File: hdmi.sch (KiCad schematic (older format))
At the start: 31 parts, among them J1901 Mini-HDMI, Q1901 NX3020NAKS, Q1902 NX3020NAKS, Q1903 NX3020NAKS, Q1904 NX3020NAKS, U1901 PCMF3HDMI2SZ, U1902 PCMF2HDMI2SZ

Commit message: Assign TLV3201AIDBVR footprint based on the SOT-23-5 official footprint using the given solder mask clearance and pad clearance parameters, assign the QFN48 3D model to the ETH PHY footprint, make some minor adjustments to the front sheet's layout
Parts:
- renumbered Q1903 to Q1901, Q1901 to Q1902, Q1903 to Q1902, Q1902 to Q1903, Q1904 to Q1903, Q1902 to Q1904
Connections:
- net 1V8_P: now also Q1901.5 (G), Q1902.2 (G), Q1903.5 (G), Q1904.2 (G); no longer Q1901.2 (G), Q1902.5 (G), Q1903.2 (G), Q1904.5 (G)
- net GND: now also Q1901.4 (S), Q1902.1 (S), Q1903.4 (S), Q1904.1 (S); no longer Q1901.1 (S), Q1902.4 (S), Q1903.1 (S), Q1904.4 (S)
- net at R1903.2: now also Q1901.3 (D); no longer Q1902.3 (D)
- net at R1905.2: now also Q1902.6 (D); no longer Q1903.6 (D)
- net at R1907.2: now also Q1902.3 (D); no longer Q1904.3 (D)
- net at R1902.2: now also Q1903.6 (D); no longer Q1901.6 (D)
- net at R1904.2: now also Q1903.3 (D); no longer Q1902.3 (D)
- net at R1906.2: now also Q1904.6 (D); no longer Q1903.6 (D)
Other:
- moved on the sheet: Q1902B, Q1903A
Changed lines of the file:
@@
 Sheet 19 24
 Title "HDMI"
-Date "2018-06-11"
+Date "2018-06-14"
 Rev "v0.1.0"
 Comp "Copyright 2018 GNU GPLv3"
@@
 $EndComp
 $Comp
-L 1V8_P #PWR0329
+L 1V8_P #PWR1901
 U 1 1 5B01672B
 P 750 3350
-F 0 "#PWR0329" H 750 3200 50  0001 C CNN
+F 0 "#PWR1901" H 750 3200 50  0001 C CNN
 F 1 "1V8_P" H 750 3490 50  0000 C CNN
 F 2 "" H 750 3350 50  0001 C CNN
@@
 $EndComp
 $Comp
-L 1V8_P #PWR0330
+L 1V8_P #PWR1902
 U 1 1 5B019D66
 P 750 5050
-F 0 "#PWR0330" H 750 4900 50  0001 C CNN
+F 0 "#PWR1902" H 750 4900 50  0001 C CNN
 F 1 "1V8_P" H 750 5190 50  0000 C CNN
 F 2 "" H 750 5050 50  0001 C CNN
@@
 ±1%!!!
 $Comp
-L GND #PWR0331
+L GND #PWR1903
 U 1 1 5B081BE1
 P 4150 3400
-F 0 "#PWR0331" H 4150 3150 50  0001 C CNN
+F 0 "#PWR1903" H 4150 3150 50  0001 C CNN
 F 1 "GND" H 4150 3250 50  0000 C CNN
 F 2 "" H 4150 3400 50  0001 C CNN
@@
 HDMI_TX1N
 $Comp
-L GND #PWR0332
+L GND #PWR1904
 U 1 1 5B08911B
 P 4150 5100
-F 0 "#PWR0332" H 4150 4850 50  0001 C CNN
+F 0 "#PWR1904" H 4150 4850 50  0001 C CNN
 F 1 "GND" H 4150 4950 50  0000 C CNN
 F 2 "" H 4150 5100 50  0001 C CNN
@@
 Layout Note:\nMay need swap some signals\ndue to micro-HDMI pinout diff\ndepending on pin location/routing
 $Comp
-L GND #PWR0333
+L GND #PWR1908
 U 1 1 5AF69B9C
 P 9200 4900
-F 0 "#PWR0333" H 9200 4650 50  0001 C CNN
+F 0 "#PWR1908" H 9200 4650 50  0001 C CNN
 F 1 "GND" H 9200 4750 50  0000 C CNN
 F 2 "" H 9200 4900 50  0001 C CNN
@@
 $EndComp
 $Comp
-L GND #PWR0334
+L GND #PWR1906
 U 1 1 5AFABCE1
 P 6150 2400
-F 0 "#PWR0334" H 6150 2150 50  0001 C CNN
+F 0 "#PWR1906" H 6150 2150 50  0001 C CNN
 F 1 "GND" H 6150 2250 50  0000 C CNN
 F 2 "" H 6150 2400 50  0001 C CNN
@@
 $EndComp
 $Comp
-L 3V3_P #PWR0335
+L 3V3_P #PWR1907
 U 1 1 5AFBD440
 P 9200 1650
-F 0 "#PWR0335" H 9200 1500 50  0001 C CNN
+F 0 "#PWR1907" H 9200 1500 50  0001 C CNN
 F 1 "3V3_P" H 9200 1790 50  0000 C CNN
 F 2 "" H 9200 1650 50  0001 C CNN
@@
 $EndComp
 $Comp
-L 5V_P #PWR0336
+L 5V_P #PWR1905
 U 1 1 5B3E4E0C
 P 6050 1800
-F 0 "#PWR0336" H 6050 1650 50  0001 C CNN
+F 0 "#PWR1905" H 6050 1650 50  0001 C CNN
 F 1 "5V_P" H 6050 1940 50  0000 C CNN
 F 2 "" H 6050 1800 50  0001 C CNN
@@
 $EndComp
 $Comp
+L Q_NMOS_DUAL Q1901
+U 2 1 5B1A7CAB
+P 1900 3100
+F 0 "Q1901" H 1550 3300 50  0000 L CNN
+F 1 "NX3020NAKS" H 1350 3200 50  0000 L CNN
+F 2 "dvk-mx8m-bsb:6-TSSOP" H 2100 3200 50  0001 C CNN
+F 3 "https://assets.nexperia.com/documents/data-sheet/NX3020NAKS.pdf" H 1900 3100 50  0001 C CNN
+F 4 "NXP" H 1900 3100 60  0001 C CNN "MFG Name"
+F 5 "NX3020NAKS" H 1900 3100 60  0001 C CNN "MFG Part Num"
+F 6 "NX3020NAKS,115" H 1900 3100 60  0001 C CNN "Distrib PN"
+F 7 "https://www.arrow.com/en/products/nx3020naks115/nexperia" H 1900 3100 60  0001 C CNN "Distrib Link"
+F 8 "-" H 1900 3100 60  0001 C CNN "Tolerance"
+F 9 "https://octopart.com/search?q=NX3020NAKS&start=0" H 1900 3100 60  0001 C CNN "Others"
+	2    1900 3100
+	1    0    0    -1
+$EndComp
+$Comp
+L Q_NMOS_DUAL Q1902
+U 1 1 5B1A8769
+P 2650 3100
+F 0 "Q1902" H 2300 3300 50  0000 L CNN
+F 1 "NX3020NAKS" H 2100 3200 50  0000 L CNN
+F 2 "dvk-mx8m-bsb:6-TSSOP" H 2850 3200 50  0001 C CNN
+F 3 "https://assets.nexperia.com/documents/data-sheet/NX3020NAKS.pdf" H 2650 3100 50  0001 C CNN
+F 4 "NXP" H 2650 3100 60  0001 C CNN "MFG Name"
+F 5 "NX3020NAKS" H 2650 3100 60  0001 C CNN "MFG Part Num"
+F 6 "NX3020NAKS,115" H 2650 3100 60  0001 C CNN "Distrib PN"
+F 7 "https://www.arrow.com/en/products/nx3020naks115/nexperia" H 2650 3100 60  0001 C CNN "Distrib Link"
+F 8 "-" H 2650 3100 60  0001 C CNN "Tolerance"
+F 9 "https://octopart.com/search?q=NX3020NAKS&start=0" H 2650 3100 60  0001 C CNN "Others"
+	1    2650 3100
+	1    0    0    -1
+$EndComp
+$Comp
 L Q_NMOS_DUAL Q1903
-U 1 1 5B1A7CAB
+U 1 1 5B1A87F5
 P 1150 4800
 F 0 "Q1903" H 800 5000 50  0000 L CNN
@@
 $EndComp
 $Comp
-L Q_NMOS_DUAL Q1901
-U 2 1 5B1A8769
-P 1900 3100
-F 0 "Q1901" H 1550 3300 50  0000 L CNN
-F 1 "NX3020NAKS" H 1350 3200 50  0000 L CNN
-F 2 "dvk-mx8m-bsb:6-TSSOP" H 2100 3200 50  0001 C CNN
-F 3 "https://assets.nexperia.com/documents/data-sheet/NX3020NAKS.pdf" H 1900 3100 50  0001 C CNN
-F 4 "NXP" H 1900 3100 60  0001 C CNN "MFG Name"
-F 5 "NX3020NAKS" H 1900 3100 60  0001 C CNN "MFG Part Num"
-F 6 "NX3020NAKS,115" H 1900 3100 60  0001 C CNN "Distrib PN"
-F 7 "https://www.arrow.com/en/products/nx3020naks115/nexperia" H 1900 3100 60  0001 C CNN "Distrib Link"
-F 8 "-" H 1900 3100 60  0001 C CNN "Tolerance"
-F 9 "https://octopart.com/search?q=NX3020NAKS&start=0" H 1900 3100 60  0001 C CNN "Others"
-	2    1900 3100
+L Q_NMOS_DUAL Q1904
+U 1 1 5B1A8AD3
+P 2650 4800
+F 0 "Q1904" H 2300 5000 50  0000 L CNN
+F 1 "NX3020NAKS" H 2100 4900 50  0000 L CNN
+F 2 "dvk-mx8m-bsb:6-TSSOP" H 2850 4900 50  0001 C CNN
+F 3 "https://assets.nexperia.com/documents/data-sheet/NX3020NAKS.pdf" H 2650 4800 50  0001 C CNN
+F 4 "NXP" H 2650 4800 60  0001 C CNN "MFG Name"
+F 5 "NX3020NAKS" H 2650 4800 60  0001 C CNN "MFG Part Num"
+F 6 "NX3020NAKS,115" H 2650 4800 60  0001 C CNN "Distrib PN"
+F 7 "https://www.arrow.com/en/products/nx3020naks115/nexperia" H 2650 4800 60  0001 C CNN "Distrib Link"
+F 8 "-" H 2650 4800 60  0001 C CNN "Tolerance"
+F 9 "https://octopart.com/search?q=NX3020NAKS&start=0" H 2650 4800 60  0001 C CNN "Others"
+	1    2650 4800
 	1    0    0    -1
 $EndComp
 $Comp
 L Q_NMOS_DUAL Q1902
-U 1 1 5B1A87F5
-P 2650 3100
-F 0 "Q1902" H 2300 3300 50  0000 L CNN
-F 1 "NX3020NAKS" H 2100 3200 50  0000 L CNN
-F 2 "dvk-mx8m-bsb:6-TSSOP" H 2850 3200 50  0001 C CNN
-F 3 "https://assets.nexperia.com/documents/data-sheet/NX3020NAKS.pdf" H 2650 3100 50  0001 C CNN
-F 4 "NXP" H 2650 3100 60  0001 C CNN "MFG Name"
-F 5 "NX3020NAKS" H 2650 3100 60  0001 C CNN "MFG Part Num"
-F 6 "NX3020NAKS,115" H 2650 3100 60  0001 C CNN "Distrib PN"
-F 7 "https://www.arrow.com/en/products/nx3020naks115/nexperia" H 2650 3100 60  0001 C CNN "Distrib Link"
-F 8 "-" H 2650 3100 60  0001 C CNN "Tolerance"
-F 9 "https://octopart.com/search?q=NX3020NAKS&start=0" H 2650 3100 60  0001 C CNN "Others"
-	1    2650 3100
-	1    0    0    -1
-$EndComp
-$Comp
-L Q_NMOS_DUAL Q1902
-U 2 1 5B1A8AD3
+U 2 1 5B1A9D21
 P 3400 3100
 F 0 "Q1902" H 3050 3300 50  0000 L CNN
@@
 $Comp
 L Q_NMOS_DUAL Q1903
-U 2 1 5B1A9D21
+U 2 1 5B1A9DC4
 P 1900 4800
 F 0 "Q1903" H 1550 5000 50  0000 L CNN
@@
 	1    0    0    -1
 $EndComp
-$Comp
-L Q_NMOS_DUAL Q1904
-U 1 1 5B1A9DC4
-P 2650 4800
-F 0 "Q1904" H 2300 5000 50  0000 L CNN
-F 1 "NX3020NAKS" H 2100 4900 50  0000 L CNN
-F 2 "dvk-mx8m-bsb:6-TSSOP" H 2850 4900 50  0001 C CNN
-F 3 "https://assets.nexperia.com/documents/data-sheet/NX3020NAKS.pdf" H 2650 4800 50  0001 C CNN
-F 4 "NXP" H 2650 4800 60  0001 C CNN "MFG Name"
-F 5 "NX3020NAKS" H 2650 4800 60  0001 C CNN "MFG Part Num"
-F 6 "NX3020NAKS,115" H 2650 4800 60  0001 C CNN "Distrib PN"
-F 7 "https://www.arrow.com/en/products/nx3020naks115/nexperia" H 2650 4800 60  0001 C CNN "Distrib Link"
-F 8 "-" H 2650 4800 60  0001 C CNN "Tolerance"
-F 9 "https://octopart.com/search?q=NX3020NAKS&start=0" H 2650 4800 60  0001 C CNN "Others"
-	1    2650 4800
-	1    0    0    -1
-$EndComp

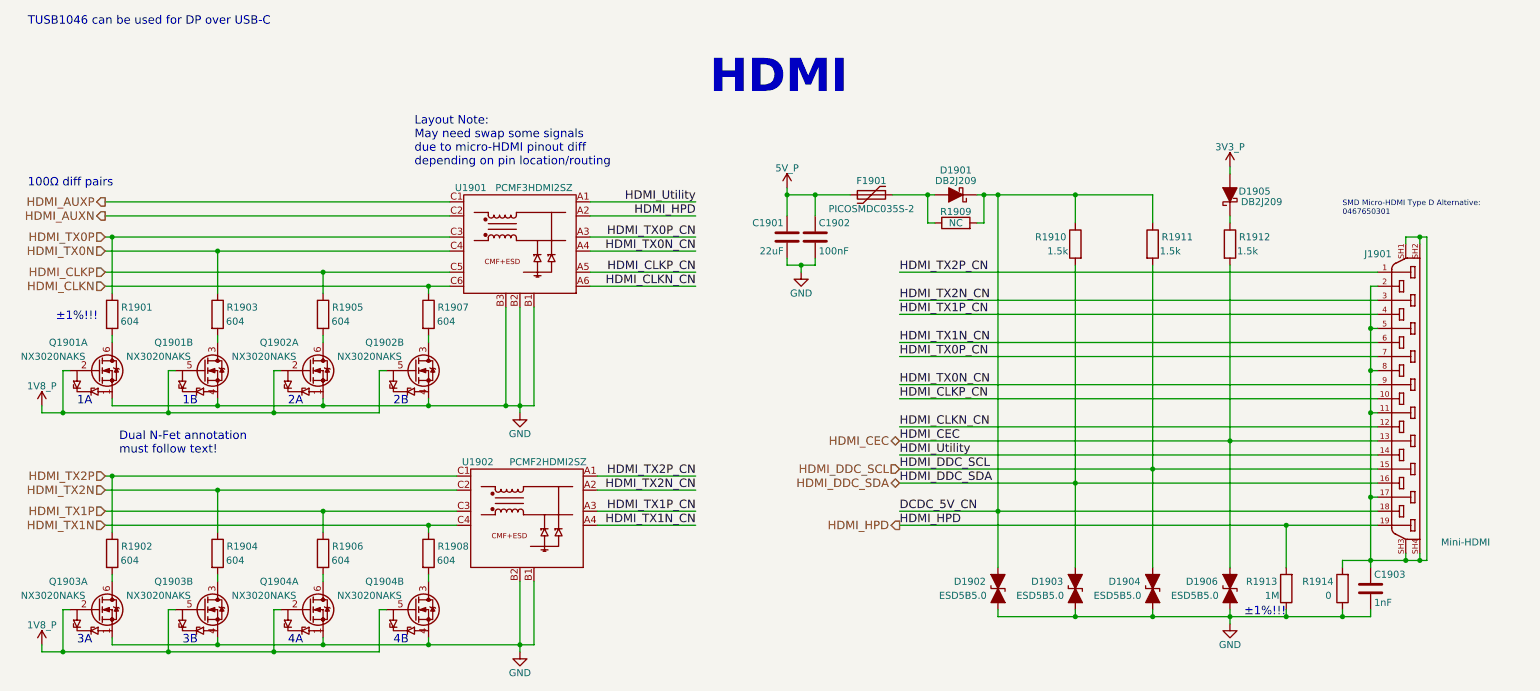
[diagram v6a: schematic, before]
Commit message: Add AC coupling caps to the HDMI_AUXP/N diff pair which were mistakenly left out, fix a couple typos/errors that were made when transitioning to the new top-leve sheet, make the M.2s' I2C RX TX hierarchical signals consistent and clearer
Hopefully all lingering errors have been caught, this will likely be the schematic commit that gets reviewed (fingers crossed).
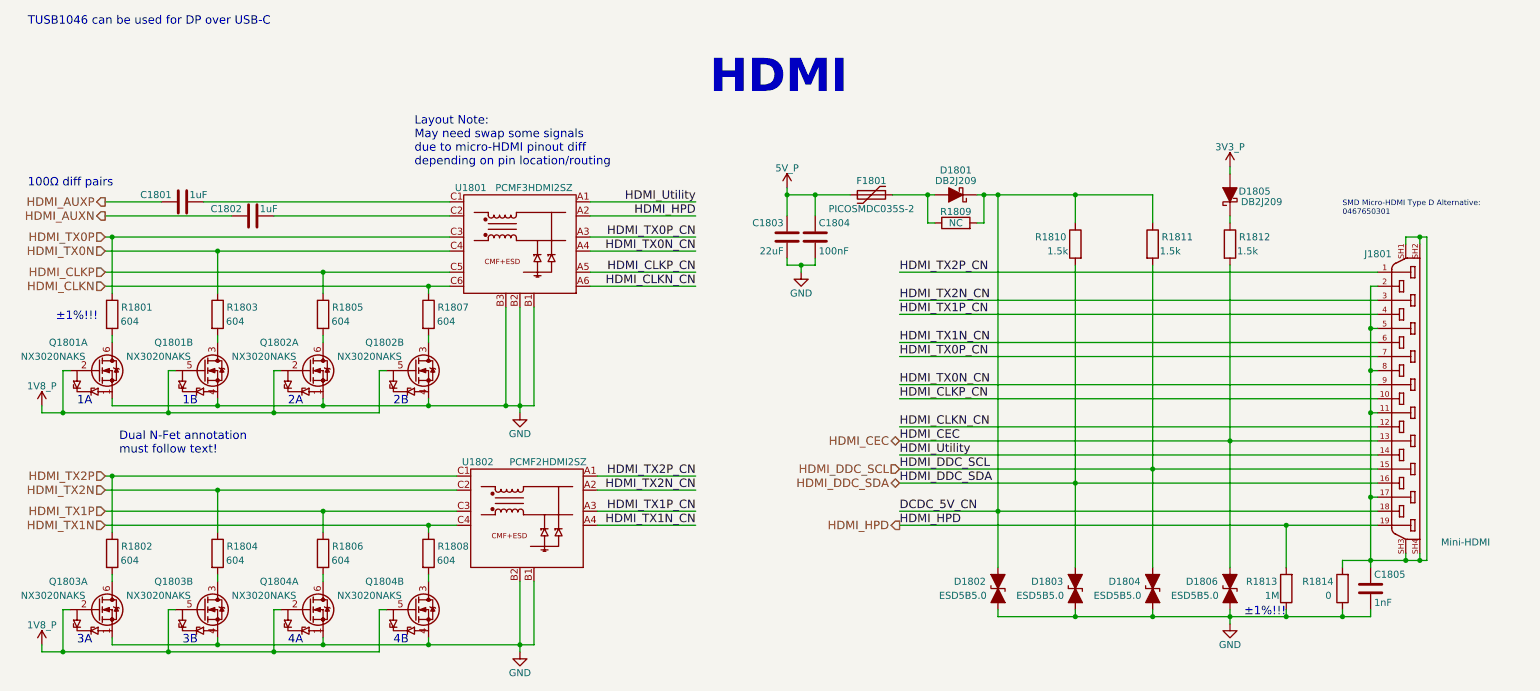
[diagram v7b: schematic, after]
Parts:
- added C1801, C1802: 1uF, symbol C
- renumbered C1901 to C1803, C1902 to C1804, C1903 to C1805, D1901 to D1801, D1902 to D1802, D1903 to D1803, D1904 to D1804, D1905 to D1805, D1906 to D1806, F1901 to F1801, J1901 to J1801, Q1901 to Q1801, Q1903 to Q1801, Q1901 to Q1802, Q1903 to Q1802, Q1902 to Q1803, Q1904 to Q1803, Q1902 to Q1804, Q1904 to Q1804, R1901 to R1801, R1902 to R1802, R1903 to R1803, R1904 to R1804, R1905 to R1805, R1906 to R1806, R1907 to R1807, R1908 to R1808, R1909 to R1809, R1910 to R1810, R1911 to R1811, R1912 to R1812, R1913 to R1813, R1914 to R1814, U1901 to U1801, U1902 to U1802
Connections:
- net 1V8_P: now also Q1801.5 (G), Q1802.2 (G), Q1803.5 (G), Q1804.2 (G); no longer Q1801.2 (G), Q1802.5 (G), Q1803.2 (G), Q1804.5 (G)
- net GND: now also Q1801.4 (S), Q1802.1 (S), Q1803.4 (S), Q1804.1 (S); no longer Q1801.1 (S), Q1802.4 (S), Q1803.1 (S), Q1804.4 (S)
- net HDMI_AUXN: now also C1802.2; no longer U1801.C2
- net HDMI_AUXP: now also C1801.2; no longer U1801.C1
- net at R1803.2: now also Q1801.3 (D); no longer Q1802.3 (D)
- net at R1805.2: now also Q1802.6 (D); no longer Q1803.6 (D)
- net at R1807.2: now also Q1802.3 (D); no longer Q1804.3 (D)
- net at R1802.2: now also Q1803.6 (D); no longer Q1801.6 (D)
- net at R1804.2: now also Q1803.3 (D); no longer Q1802.3 (D)
- net at R1806.2: now also Q1804.6 (D); no longer Q1803.6 (D)
- new net: C1801.1, U1801.C1
- new net: C1802.1, U1801.C2
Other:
- moved on the sheet: Q1802B, Q1803A

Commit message: Move the WLAN+BT M.2 sheet back to page 18 rather than the last page (24)
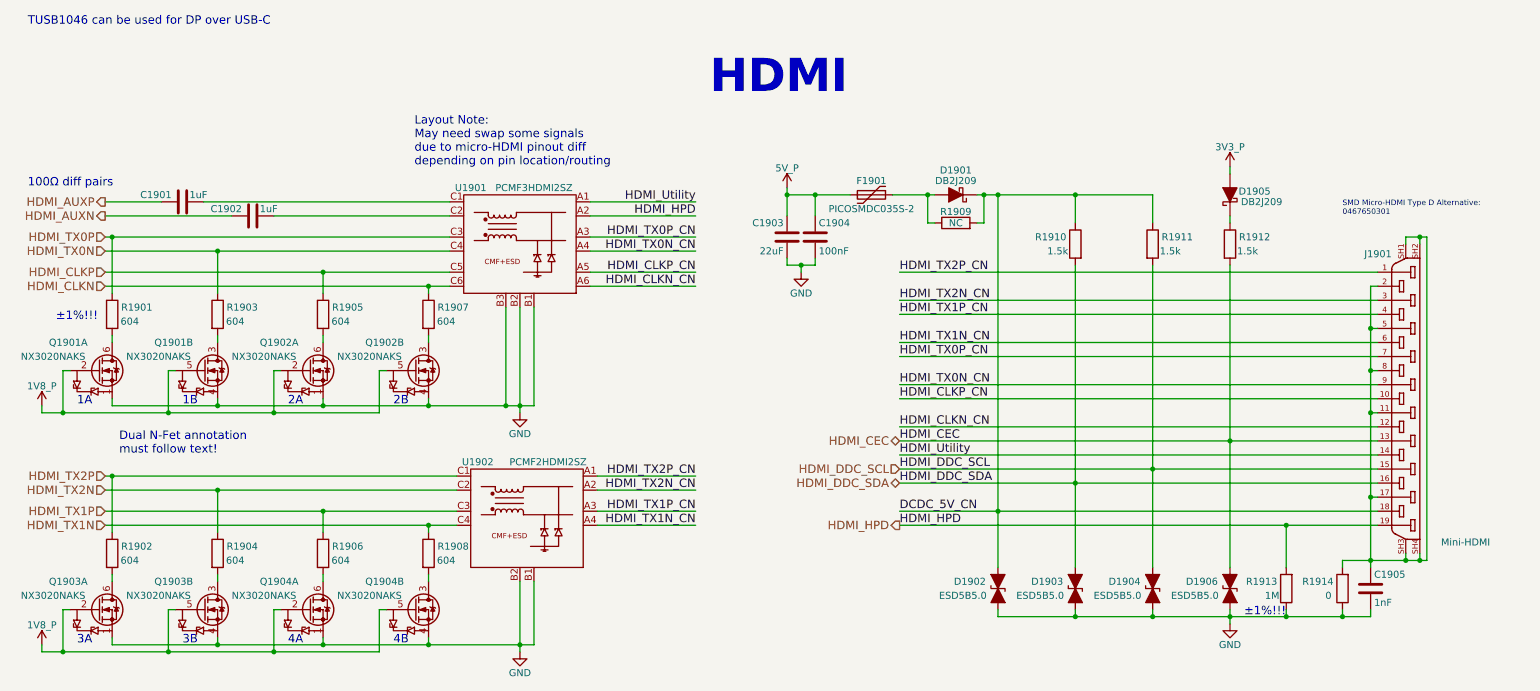
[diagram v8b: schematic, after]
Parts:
- renumbered C1801 to C1901, C1802 to C1902, C1803 to C1903, C1804 to C1904, C1805 to C1905, D1801 to D1901, D1802 to D1902, D1803 to D1903, D1804 to D1904, D1805 to D1905, D1806 to D1906, F1801 to F1901, J1801 to J1901, Q1801 to Q1901, Q1803 to Q1902, Q1802 to Q1903, Q1804 to Q1904, R1801 to R1901, R1802 to R1902, R1803 to R1903, R1804 to R1904, R1805 to R1905, R1806 to R1906, R1807 to R1907, R1808 to R1908, R1809 to R1909, R1810 to R1910, R1811 to R1911, R1812 to R1912, R1813 to R1913, R1814 to R1914, U1801 to U1901, U1802 to U1902
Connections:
- net at R1905.2: now also Q1902.6 (D); no longer Q1903.6 (D)
- net at R1907.2: now also Q1902.3 (D); no longer Q1903.3 (D)
- net at R1902.2: now also Q1903.6 (D); no longer Q1902.6 (D)
- net at R1904.2: now also Q1903.3 (D); no longer Q1902.3 (D)
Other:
- moved on the sheet: Q1902A, Q1902B, Q1903A, Q1903B
